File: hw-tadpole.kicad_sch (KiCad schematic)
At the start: 19 parts, among them J1 Screw_Terminal_01x02, J2 Conn_01x04_Socket, U1 ESP32-WROOM-32

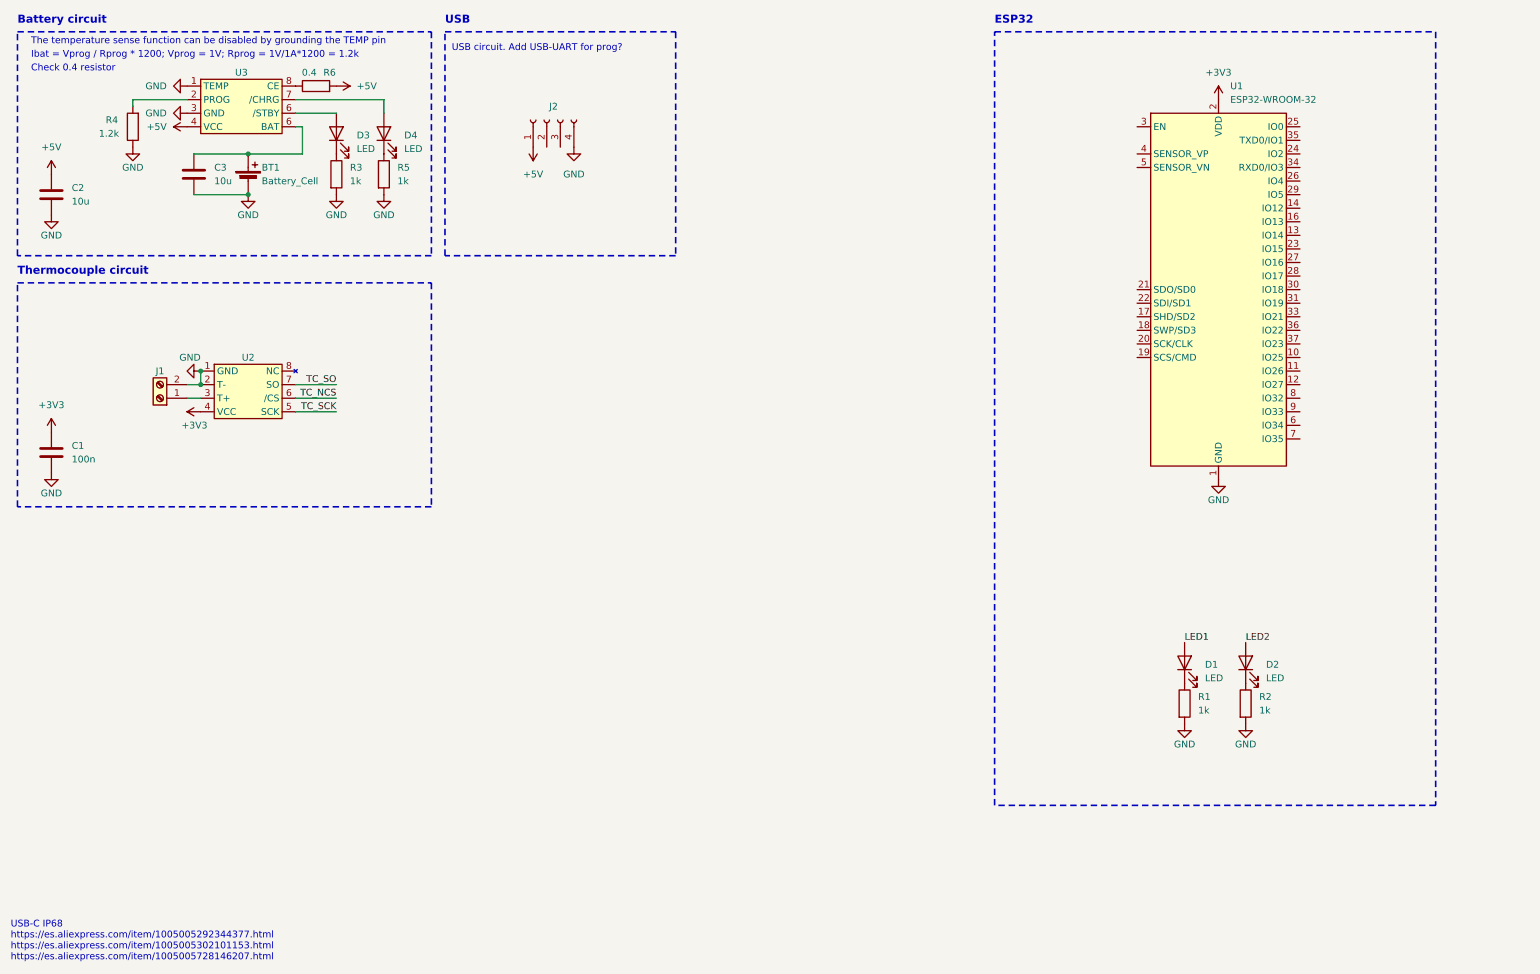
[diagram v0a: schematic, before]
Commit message: Add LoRa module and DCDC to sch
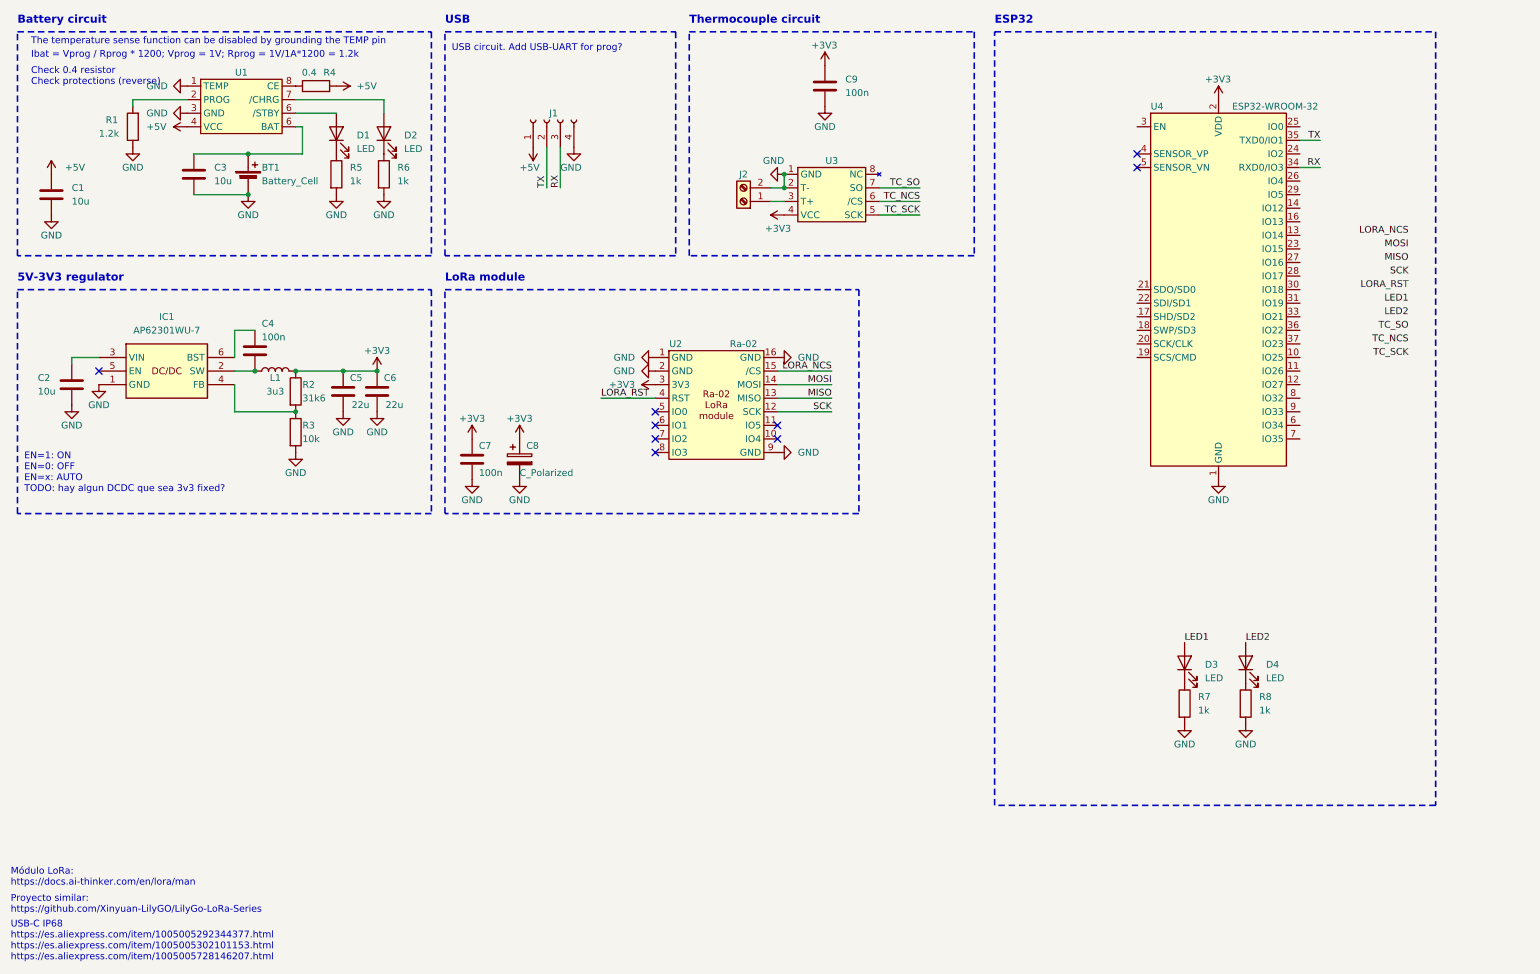
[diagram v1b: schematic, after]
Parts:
- added C2: 10u, symbol Device:C
- added C4, C7: 100n, Capacitor_SMD:C_0402_1005Metric, symbol Device:C
- added C5, C6: 22u, symbol Device:C
- added C8: C_Polarized, symbol Device:C_Polarized
- added IC1: AP62301WU-7, guille-lib:SOT95P280X100-6N, symbol guille-lib:AP62301WU-7
- added L1: 3u3, symbol Device:L
- added R2: 31k6, Capacitor_SMD:C_0402_1005Metric, symbol Device:R
- added R3: 10k, Capacitor_SMD:C_0402_1005Metric, symbol Device:R
- added U2: Ra-02, guille-lib:Ra-02, symbol guille-lib:Ra-02
- C9: renamed from C1; footprint (none) -> Capacitor_SMD:C_0402_1005Metric
- R1: renamed from R4; footprint (none) -> Capacitor_SMD:C_0402_1005Metric
- R5: renamed from R3; footprint (none) -> Capacitor_SMD:C_0402_1005Metric
- R6: renamed from R5; footprint (none) -> Capacitor_SMD:C_0402_1005Metric
- R7: renamed from R1; footprint (none) -> Capacitor_SMD:C_0402_1005Metric
- R8: renamed from R2; footprint (none) -> Capacitor_SMD:C_0402_1005Metric
- renumbered C2 to C1, D3 to D1, D4 to D2, D1 to D3, D2 to D4, J2 to J1, J1 to J2, R6 to R4, U3 to U1, U2 to U3, U1 to U4
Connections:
- net +3V3: now also C5.1, C6.1, C7.1, C8.1, L1.2, R2.1, U2.3 (3V3)
- net GND: now also C2.2, C5.2, C6.2, C7.2, C8.2, IC1.1 (GND), R3.2, U2.1 (GND), U2.16 (GND), U2.2 (GND), U2.9 (GND)
- net RX: now reaches U4.34 (RXD0/IO3)
- net RX: now also J1.3 (Pin_3)
- net TX: now reaches U4.35 (TXD0/IO1)
- net TX: now also J1.2 (Pin_2)
- new net: C4.2, IC1.2 (SW), L1.1
- new net: C2.1, IC1.3 (VIN)
- new net: IC1.4 (FB), R2.2, R3.1
- new net: C4.1, IC1.6 (BST)
- new net LORA_NCS: U2.15 (/CS)
- new net LORA_RST: U2.4 (RST)
- new net MISO: U2.13 (MISO)
- new net MOSI: U2.14 (MOSI)
- new net SCK: U2.12 (SCK)
- no-connect marks 0 -> 9
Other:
- note added: "5V-3V3 regulator"
- note added: "Check 0.4 resistor Check protections (reverse)"
- note added: "EN=1: ON EN=0: OFF EN=x: AUTO TODO: hay algun DCDC que sea 3v3 fixed?"
- note added: "LoRa module"
- note added: "Módulo LoRa: https://docs.ai-thinker.com/en/lora/man"
- note added: "Proyecto similar: https://github.com/Xinyuan-LilyGO/LilyGo-LoRa-Series"
- note removed: "Check 0.4 resistor"
- moved on the sheet: C9, J2, U3

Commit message: Add battery holder and USB-UART
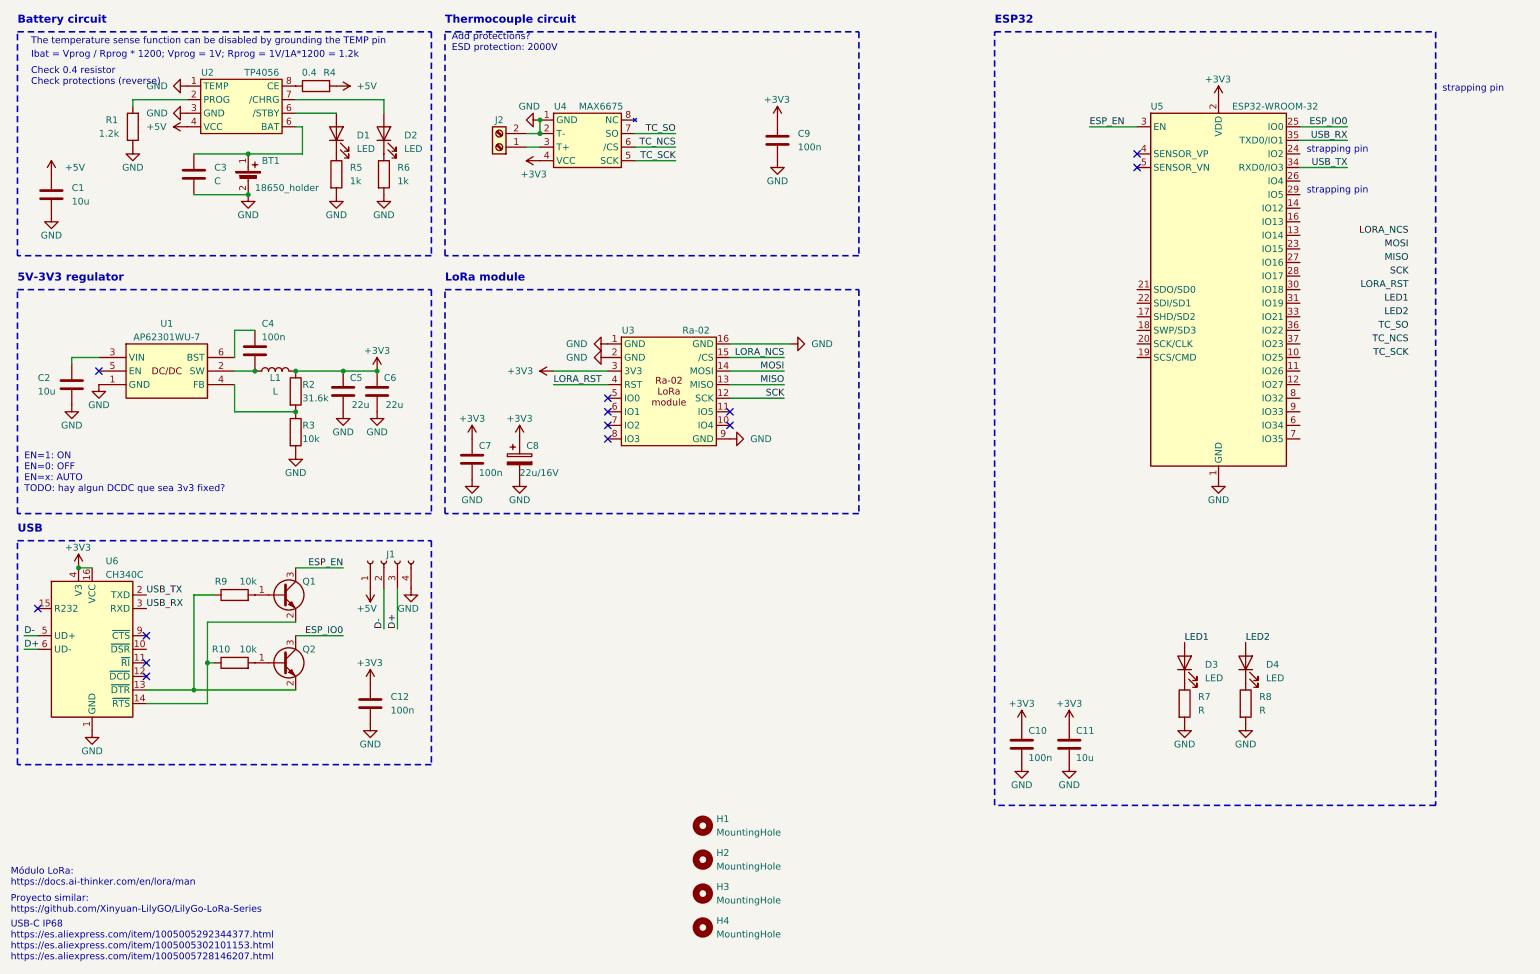
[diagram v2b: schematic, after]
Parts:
- removed BT1: Battery_Cell, symbol Device:Battery_Cell
- added BT1: 18650_holder, guille-lib:18650_HOLDER_AliExpress, symbol guille-lib:18650_HOLDER_AliExpress
- added C10, C12: 100n, Capacitor_SMD:C_0402_1005Metric, symbol Device:C
- added C11: 10u, Capacitor_SMD:C_0805_2012Metric, symbol Device:C
- added H1, H2, H3, H4: MountingHole, MountingHole:MountingHole_2.2mm_M2, symbol Mechanical:MountingHole
- added Q1, Q2: PMBT3904235, Package_TO_SOT_SMD:SOT-23, symbol guille-lib:PMBT3904235
- added R10, R9: 10k, symbol Device:R
- added U6: CH340C, Package_SO:SOIC-16_3.9x9.9mm_P1.27mm, symbol Interface_USB:CH340C
- C1, C2, C5, C6: footprint (none) -> Capacitor_SMD:C_0805_2012Metric
- C3: value 10u -> C; footprint (none) -> Capacitor_SMD:C_0805_2012Metric
- C8: value C_Polarized -> 22u/16V
- D1, D2, D3, D4: footprint (none) -> LED_THT:LED_D3.0mm
- J1: footprint (none) -> Connector_PinSocket_2.54mm:PinSocket_1x04_P2.54mm_Vertical
- J2: footprint (none) -> Connector_Phoenix_MSTB:PhoenixContact_MSTBA_2,5_2-G-5,08_1x02_P5.08mm_Horizontal
- L1: value 3u3 -> L
- R1, R3, R5, R6: footprint Capacitor_SMD:C_0402_1005Metric -> Resistor_SMD:R_0402_1005Metric
- R2: value 31k6 -> 31.6k; footprint Capacitor_SMD:C_0402_1005Metric -> Resistor_SMD:R_0402_1005Metric
- R4: footprint (none) -> Resistor_SMD:R_0402_1005Metric
- R7, R8: value 1k -> R; footprint Capacitor_SMD:C_0402_1005Metric -> Resistor_SMD:R_0402_1005Metric
- U2: renamed from U1; value ~ -> TP4056
- U4: renamed from U3; value ~ -> MAX6675
- renumbered IC1 to U1, U2 to U3, U4 to U5
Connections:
- net +3V3: now also C10.1, C11.1, C12.1, U6.16 (VCC), U6.4 (V3)
- net GND: now also BT1.2, C10.2, C11.2, C12.2, U6.1 (GND)
- net at C3.1, U2.6 (BAT): now also BT1.1
- net ESP_IO0: now reaches U5.25 (IO0)
- net ESP_IO0: now also Q2.3
- net ESP_EN: now reaches U5.3 (EN)
- net ESP_EN: now also Q1.3
- net RX renamed D+
- net D+: now also U6.6 (UD-); no longer U5.34 (RXD0/IO3)
- net TX renamed D-
- net D-: now also U6.5 (UD+); no longer U5.35 (TXD0/IO1)
- new net: Q1.2, R10.1, U6.14 (~{RTS})
- new net: Q2.1, R10.2
- new net: Q2.2, R9.1, U6.13 (~{DTR})
- new net: Q1.1, R9.2
- new net USB_RX: U5.35 (TXD0/IO1), U6.3 (RXD)
- new net USB_TX: U5.34 (RXD0/IO3), U6.2 (TXD)
- no-connect marks 9 -> 13
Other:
- note added: "Add protections? ESD protection: 2000V"
- note added: "strapping pin"
- note removed: "USB circuit. Add USB-UART for prog?"
- moved on the sheet: C9, J1, J2, U3, U4

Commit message: Add ESP32-S2-SOLO
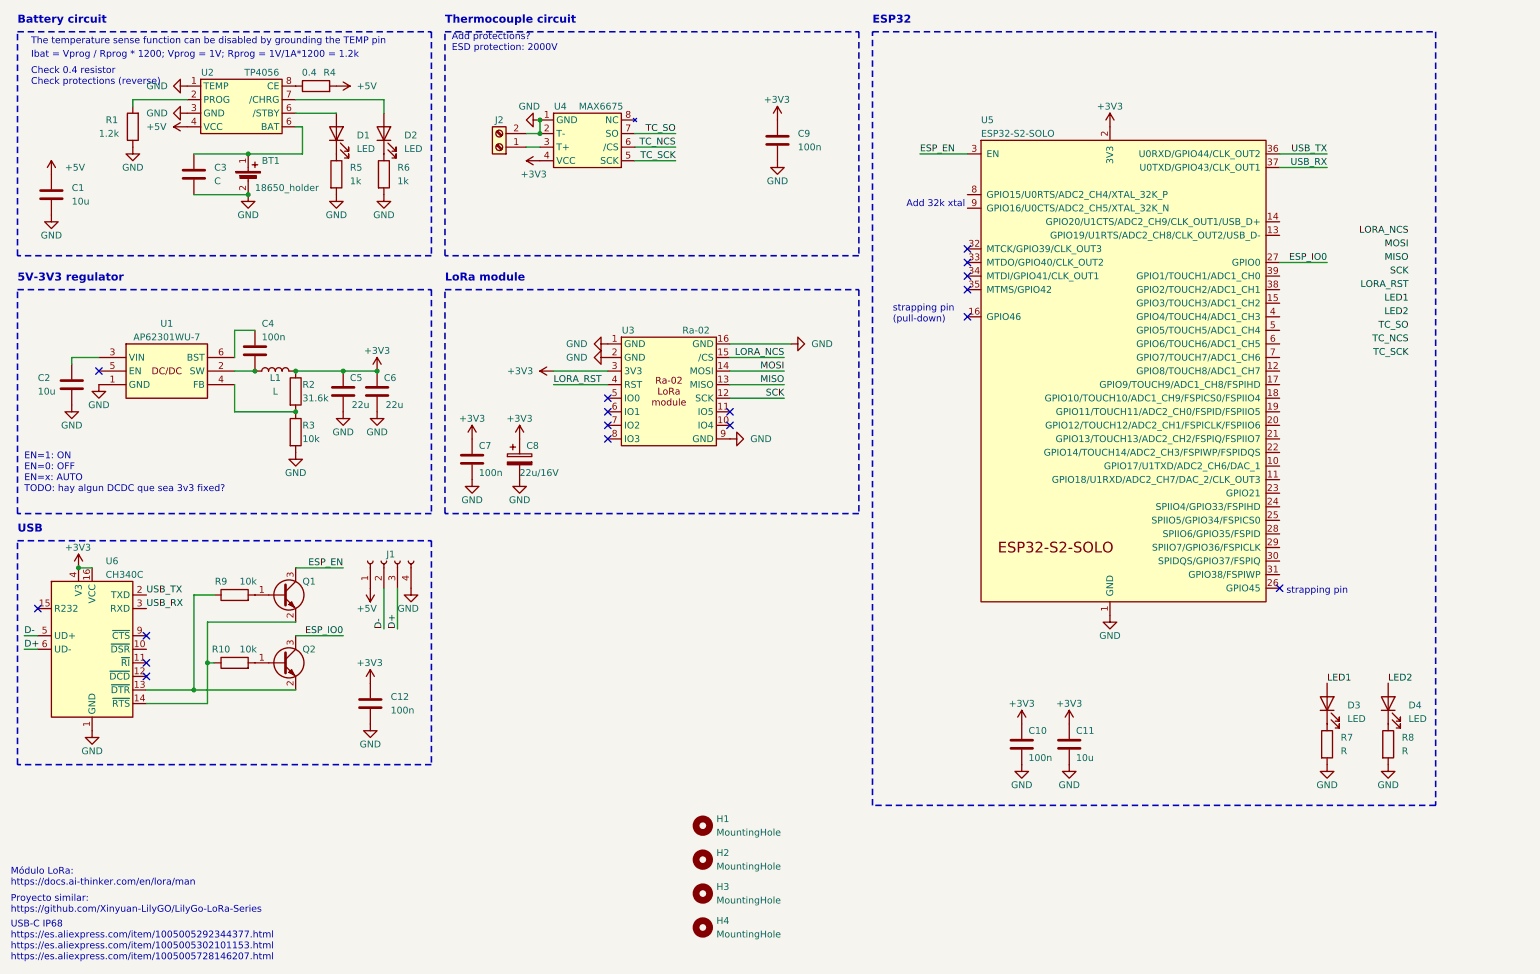
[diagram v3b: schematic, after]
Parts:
- removed U5: ESP32-WROOM-32, RF_Module:ESP32-WROOM-32, symbol RF_Module:ESP32-WROOM-32
- added U5: ESP32-S2-SOLO, PCM_Espressif:ESP32-S2-SOLO, symbol guille-lib:ESP32-S2-SOLO
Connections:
- net +3V3: now also U5.2 (3V3)
- net ESP_EN: now also U5.3 (EN)
- net ESP_IO0: now also U5.27 (GPIO0)
- net GND: now also U5.1 (GND), U5.40 (GND), U5.41 (GND)
- net USB_RX: now also U5.37 (U0TXD/GPIO43/CLK_OUT1)
- net USB_TX: now also U5.36 (U0RXD/GPIO44/CLK_OUT2)
- no-connect marks 13 -> 17
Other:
- note added: "Add 32k xtal"
- note added: "strapping pin (pull-down)"
- moved on the sheet: D3, D4, R7, R8

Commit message: Add a BMS and continue with sch
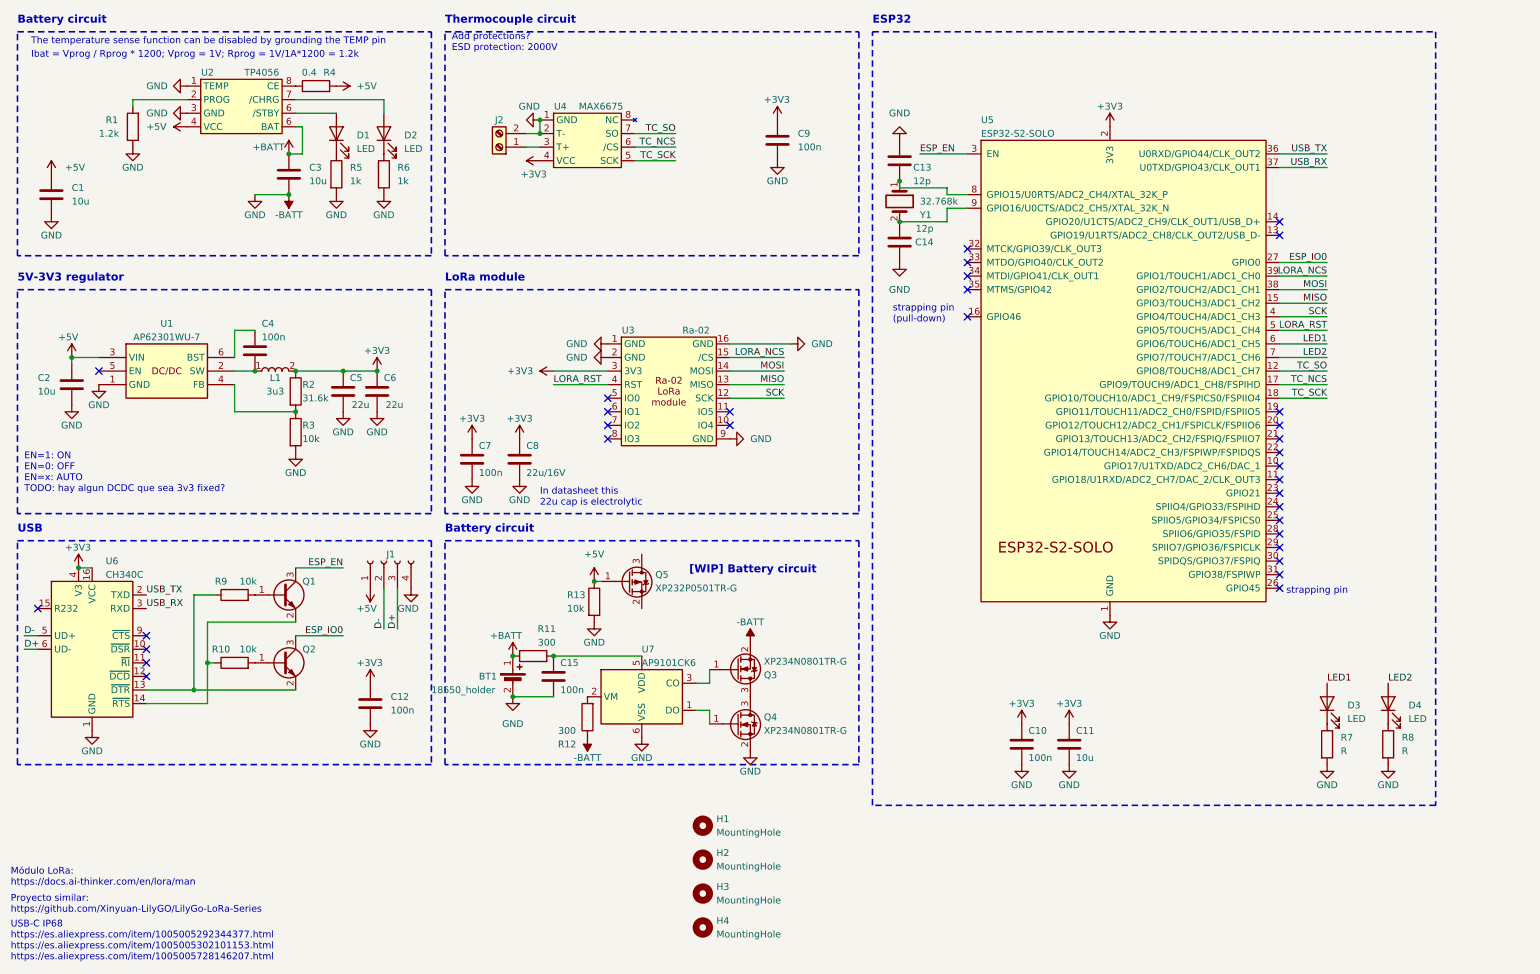
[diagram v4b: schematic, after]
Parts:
- removed C8: 22u/16V, symbol Device:C_Polarized
- removed L1: L, symbol Device:L
- added C13, C14: 12p, Capacitor_SMD:C_0402_1005Metric, symbol Device:C
- added C15: 100n, Capacitor_SMD:C_0402_1005Metric, symbol Device:C
- added C8: 22u/16V, Capacitor_SMD:C_0402_1005Metric, symbol Device:C
- added L1: 3u3, guille-lib:SRN5020TA3R3M, symbol guille-lib:SRN5020TA-3R3M
- added Q3, Q4: XP234N0801TR-G, guille-lib:SOT-23-3, symbol guille-lib:XP234N0801TR-G
- added Q5: XP232P0501TR-G, guille-lib:SOT-23-3, symbol guille-lib:XP232P0501TR-G
- added R11, R12: 300, Resistor_SMD:R_0402_1005Metric, symbol Device:R
- added R13: 10k, Resistor_SMD:R_0402_1005Metric, symbol Device:R
- added U7: AP9101CK6, Package_TO_SOT_SMD:SOT-23-6, symbol Battery_Management:AP9101CK6
- added Y1: 32.768k, guille-lib:SC32S7PF20PPM, symbol guille-lib:SC32S-7PF20PPM
- C3: value C -> 10u
- R10, R9: footprint (none) -> Resistor_SMD:R_0402_1005Metric
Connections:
- net +3V3: now also C8.1, L1.2
- net +5V: now also C2.1, U1.3 (VIN), Q5.1, R13.1
- net LED1: now also U5.6 (GPIO6/TOUCH6/ADC1_CH5)
- net LED2: now also U5.7 (GPIO7/TOUCH7/ADC1_CH6)
- net LORA_NCS: now also U5.39 (GPIO1/TOUCH1/ADC1_CH0)
- net LORA_RST: now also U5.5 (GPIO5/TOUCH5/ADC1_CH4)
- net MISO: now also U5.15 (GPIO3/TOUCH3/ADC1_CH2)
- net MOSI: now also U5.38 (GPIO2/TOUCH2/ADC1_CH1)
- net SCK: now also U5.4 (GPIO4/TOUCH4/ADC1_CH3)
- net TC_NCS: now also U5.17 (GPIO9/TOUCH9/ADC1_CH8/FSPIHD)
- net TC_SCK: now also U5.18 (GPIO10/TOUCH10/ADC1_CH9/FSPICS0/FSPIIO4)
- net TC_SO: now also U5.12 (GPIO8/TOUCH8/ADC1_CH7)
- net at C4.2, U1.2 (SW): now also L1.1
- net at U5.8 (GPIO15/U0RTS/ADC2_CH4/XTAL_32K_P): now also C13.2, Y1.1
- net at U5.9 (GPIO16/U0CTS/ADC2_CH5/XTAL_32K_N): now also C14.2, Y1.2
- net +BATT: now reaches BT1.1, C3.1, U2.6 (BAT)
- net +BATT: now also R11.1
- net GND renamed -BATT
- net -BATT: now also C13.1, C14.1, C15.2, C8.2, Q3.2, Q4.2, R12.1, R13.2, U7.6 (VSS)
- new net: R12.2, U7.2 (VM)
- new net: Q3.1, U7.3 (CO)
- new net: Q3.3, Q4.3
- new net: C15.1, R11.2, U7.5 (VDD)
- new net: Q4.1, U7.1 (DO)
- no-connect marks 17 -> 33
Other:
- note added: "In datasheet this 22u cap is electrolytic"
- note added: "[WIP] Battery circuit"
- note removed: "Add 32k xtal"
- note removed: "Check 0.4 resistor Check protections (reverse)"
- moved on the sheet: BT1, C3
